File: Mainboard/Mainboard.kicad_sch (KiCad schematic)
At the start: 0 parts

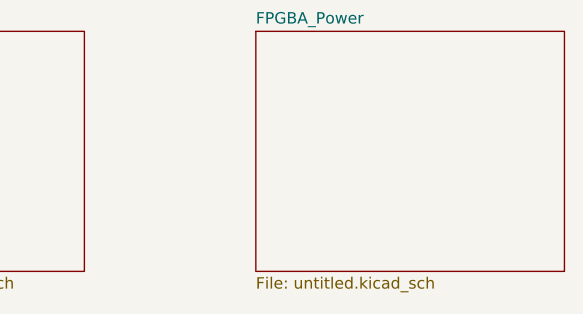
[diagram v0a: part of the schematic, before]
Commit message: fixed heirarchy and dir structure
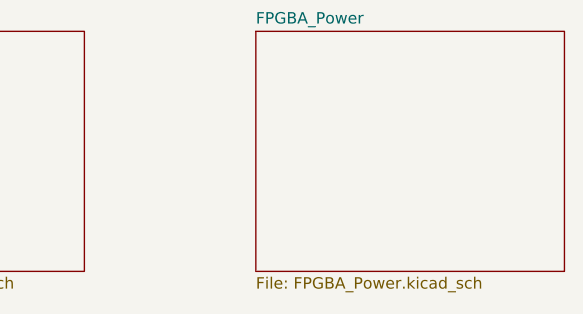
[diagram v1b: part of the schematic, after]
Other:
- sheet FPGBA_Power: file untitled.kicad_sch -> FPGBA_Power.kicad_sch
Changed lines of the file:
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@@
 			)
 		)
-		(property "Sheetfile" "untitled.kicad_sch"
+		(property "Sheetfile" "FPGBA_Power.kicad_sch"
 			(at 85.09 64.0846 0)
 			(show_name no)

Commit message: huge update: power/charging, audio, zif connections, screen, cartridge pinout
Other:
- added sheet Screen (screen.kicad_sch)
- added sheet Spartan 7 (spartan7.kicad_sch)
- added sheet speaker (speaker.kicad_sch)
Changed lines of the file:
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@@
 	(paper "A4")
+	(sheet
+		(at 142.24 35.56)
+		(size 34.29 25.4)
+		(exclude_from_sim no)
+		(in_bom yes)
+		(on_board yes)
+		(dnp no)
+		(fields_autoplaced yes)
+		(stroke
+			(width 0.1524)
+			(type solid)
+		)
+		(fill
+			(color 0 0 0 0)
+		)
+		(property "Sheetname" "Spartan 7"
+			(at 142.24 34.8484 0)
+			(show_name no)
+			(do_not_autoplace no)
+			(effects
+				(font
+					(size 1.27 1.27)
+				)
+				(justify left bottom)
+			)
+		)
+		(property "Sheetfile" "spartan7.kicad_sch"
+			(at 142.24 61.5446 0)
+			(show_name no)
+			(do_not_autoplace no)
+			(effects
+				(font
+					(size 1.27 1.27)
+				)
+				(justify left top)
+			)
+		)
+		(instances
+			(project "Mainboard"
+				(path "/53a66bf0-ca24-4129-bc39-ed3123c0a797"
+					(page "4")
+				)
+			)
+		)
+	)
+	(sheet
+		(at 85.09 81.28)
+		(size 34.29 22.86)
+		(exclude_from_sim no)
+		(in_bom yes)
+		(on_board yes)
+		(dnp no)
+		(fields_autoplaced yes)
+		(stroke
+			(width 0.1524)
+			(type solid)
+		)
+		(fill
+			(color 0 0 0 0)
+		)
+		(property "Sheetname" "speaker"
+			(at 85.09 80.5684 0)
+			(show_name no)
+			(do_not_autoplace no)
+			(effects
+				(font
+					(size 1.27 1.27)
+				)
+				(justify left bottom)
+			)
+		)
+		(property "Sheetfile" "speaker.kicad_sch"
+			(at 85.09 104.7246 0)
+			(show_name no)
+			(do_not_autoplace no)
+			(effects
+				(font
+					(size 1.27 1.27)
+				)
+				(justify left top)
+			)
+		)
+		(instances
+			(project "Mainboard"
+				(path "/53a66bf0-ca24-4129-bc39-ed3123c0a797"
+					(page "6")
+				)
+			)
+		)
+	)
 	(sheet
 		(at 85.09 36.83)
@@
 				)
 			)
+		)
+	)
+	(sheet
+		(at 30.48 81.28)
+		(size 34.29 22.86)
+		(exclude_from_sim no)
+		(in_bom yes)
+		(on_board yes)
+		(dnp no)
+		(fields_autoplaced yes)
+		(stroke
+			(width 0.1524)
+			(type solid)
+		)
+		(fill
+			(color 0 0 0 0)
+		)
+		(property "Sheetname" "Screen"
+			(at 30.48 80.5684 0)
+			(show_name no)
+			(do_not_autoplace no)
+			(effects
+				(font
+					(size 1.27 1.27)
+				)
+				(justify left bottom)
+			)
+		)
+		(property "Sheetfile" "screen.kicad_sch"
+			(at 30.48 104.7246 0)
+			(show_name no)
+			(do_not_autoplace no)
+			(effects
+				(font
+					(size 1.27 1.27)
+				)
+				(justify left top)
+			)
+		)
+		(instances
+			(project "Mainboard"
+				(path "/53a66bf0-ca24-4129-bc39-ed3123c0a797"
+					(page "5")
+				)
+			)

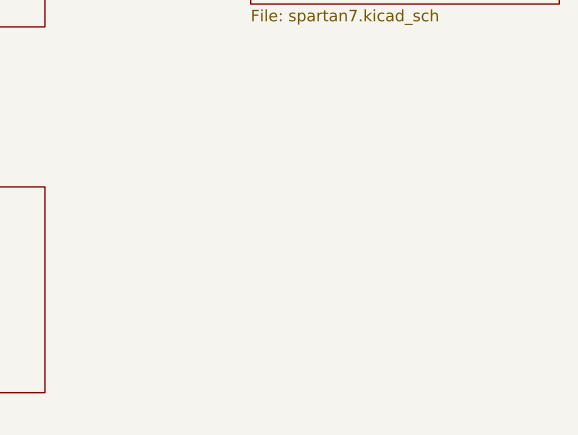
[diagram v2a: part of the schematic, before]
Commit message: added JTAG + QSPI traces to PCB
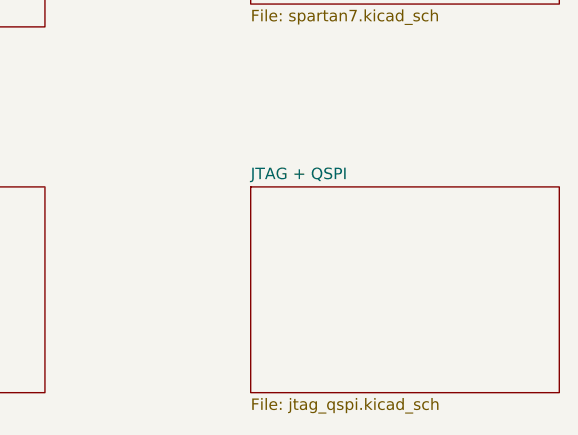
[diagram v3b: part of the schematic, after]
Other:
- added sheet JTAG + QSPI (jtag_qspi.kicad_sch)
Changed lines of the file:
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@@
+	)
+	(sheet
+		(at 142.24 81.28)
+		(size 34.29 22.86)
+		(exclude_from_sim no)
+		(in_bom yes)
+		(on_board yes)
+		(dnp no)
+		(fields_autoplaced yes)
+		(stroke
+			(width 0.1524)
+			(type solid)
+		)
+		(fill
+			(color 0 0 0 0)
+		)
+		(property "Sheetname" "JTAG + QSPI"
+			(at 142.24 80.5684 0)
+			(show_name no)
+			(do_not_autoplace no)
+			(effects
+				(font
+					(size 1.27 1.27)
+				)
+				(justify left bottom)
+			)
+		)
+		(property "Sheetfile" "jtag_qspi.kicad_sch"
+			(at 142.24 104.7246 0)
+			(show_name no)
+			(do_not_autoplace no)
+			(effects
+				(font
+					(size 1.27 1.27)
+				)
+				(justify left top)
+			)
+		)
+		(instances
+			(project "Mainboard"
+				(path "/53a66bf0-ca24-4129-bc39-ed3123c0a797"
+					(page "7")
+				)
+			)
+		)
 	)
 	(sheet

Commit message: FPGA schematic and board images
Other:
- added sheet FPGA (fpga_sch.kicad_sch)
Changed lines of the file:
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@@
+	)
+	(sheet
+		(at 182.88 35.56)
+		(size 36.83 25.4)
+		(exclude_from_sim no)
+		(in_bom yes)
+		(on_board yes)
+		(dnp no)
+		(fields_autoplaced yes)
+		(stroke
+			(width 0.1524)
+			(type solid)
+		)
+		(fill
+			(color 0 0 0 0)
+		)
+		(property "Sheetname" "FPGA"
+			(at 182.88 34.8484 0)
+			(show_name no)
+			(do_not_autoplace no)
+			(effects
+				(font
+					(size 1.27 1.27)
+				)
+				(justify left bottom)
+			)
+		)
+		(property "Sheetfile" "fpga_sch.kicad_sch"
+			(at 182.88 61.5446 0)
+			(show_name no)
+			(do_not_autoplace no)
+			(effects
+				(font
+					(size 1.27 1.27)
+				)
+				(justify left top)
+			)
+		)
+		(instances
+			(project "Mainboard"
+				(path "/53a66bf0-ca24-4129-bc39-ed3123c0a797"
+					(page "8")
+				)
+			)
+		)
 	)
 	(sheet
